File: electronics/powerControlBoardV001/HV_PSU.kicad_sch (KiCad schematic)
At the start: 0 parts

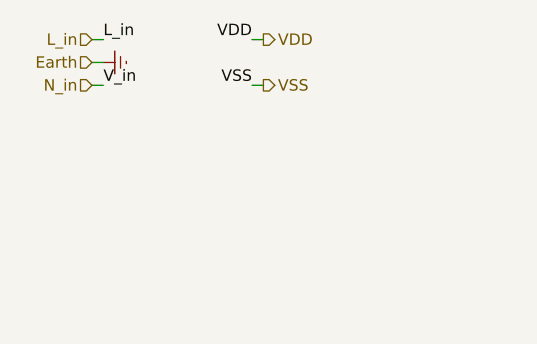
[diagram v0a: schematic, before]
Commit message: added hv psu section
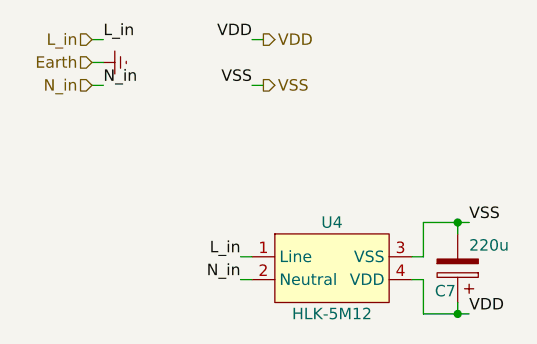
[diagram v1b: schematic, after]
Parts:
- added C7: 220u, Capacitor_THT:CP_Radial_D10.0mm_P5.00mm, symbol Device:C_Polarized
- added U4: HLK-5M12, SquantorHi-link:5MXX_series, symbol SquantorHi-link:power_module
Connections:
- net L_in: now also U4.1 (Line)
- net N_in: now also U4.2 (Neutral)
- net VDD: now also C7.1, U4.4 (VDD)
- net VSS: now also C7.2, U4.3 (VSS)
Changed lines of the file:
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@@
 (kicad_sch (version 20211123) (generator eeschema)
   (paper "A4")
+  (junction (at 60.96 48.26) (diameter 0) (color 0 0 0 0)
+  )
+  (junction (at 60.96 38.1) (diameter 0) (color 0 0 0 0)
+  )
+  (wire (pts (xy 60.96 38.1) (xy 60.96 39.37))
+    (stroke (width 0) (type default) (color 0 0 0 0))
+  )
   (wire (pts (xy 38.1 22.86) (xy 39.37 22.86))
+    (stroke (width 0) (type default) (color 0 0 0 0))
+  )
+  (wire (pts (xy 57.15 38.1) (xy 60.96 38.1))
+    (stroke (width 0) (type default) (color 0 0 0 0))
+  )
+  (wire (pts (xy 36.83 41.91) (xy 38.1 41.91))
+    (stroke (width 0) (type default) (color 0 0 0 0))
+  )
+  (wire (pts (xy 57.15 44.45) (xy 57.15 48.26))
     (stroke (width 0) (type default) (color 0 0 0 0))
   )
@@
     (stroke (width 0) (type default) (color 0 0 0 0))
   )
+  (wire (pts (xy 36.83 44.45) (xy 38.1 44.45))
+    (stroke (width 0) (type default) (color 0 0 0 0))
+  )
   (wire (pts (xy 21.59 22.86) (xy 20.32 22.86))
+    (stroke (width 0) (type default) (color 0 0 0 0))
+  )
+  (wire (pts (xy 60.96 46.99) (xy 60.96 48.26))
     (stroke (width 0) (type default) (color 0 0 0 0))
   )
@@
     (stroke (width 0) (type default) (color 0 0 0 0))
   )
+  (wire (pts (xy 60.96 48.26) (xy 62.23 48.26))
+    (stroke (width 0) (type default) (color 0 0 0 0))
+  )
+  (wire (pts (xy 57.15 41.91) (xy 57.15 38.1))
+    (stroke (width 0) (type default) (color 0 0 0 0))
+  )
+  (wire (pts (xy 55.88 41.91) (xy 57.15 41.91))
+    (stroke (width 0) (type default) (color 0 0 0 0))
+  )
+  (wire (pts (xy 55.88 44.45) (xy 57.15 44.45))
+    (stroke (width 0) (type default) (color 0 0 0 0))
+  )
+  (wire (pts (xy 57.15 48.26) (xy 60.96 48.26))
+    (stroke (width 0) (type default) (color 0 0 0 0))
+  )
+  (wire (pts (xy 60.96 38.1) (xy 62.23 38.1))
+    (stroke (width 0) (type default) (color 0 0 0 0))
+  )
   (label "VSS" (at 38.1 22.86 180)
     (effects (font (size 1.27 1.27)) (justify right bottom))
   )
-  (label "V_in" (at 21.59 22.86 0)
+  (label "L_in" (at 36.83 41.91 180)
+    (effects (font (size 1.27 1.27)) (justify right bottom))
+  )
+  (label "VSS" (at 62.23 38.1 0)
+    (effects (font (size 1.27 1.27)) (justify left bottom))
+  )
+  (label "N_in" (at 21.59 22.86 0)
     (effects (font (size 1.27 1.27)) (justify left bottom))
   )
@@
   (label "VDD" (at 38.1 17.78 180)
     (effects (font (size 1.27 1.27)) (justify right bottom))
+  )
+  (label "N_in" (at 36.83 44.45 180)
+    (effects (font (size 1.27 1.27)) (justify right bottom))
+  )
+  (label "VDD" (at 62.23 48.26 0)
+    (effects (font (size 1.27 1.27)) (justify left bottom))
   )
   (hierarchical_label "VSS" (shape output) (at 39.37 22.86 0)
@@
     (pin "1")
   )
+  (symbol (lib_id "SquantorHi-link:power_module") (at 46.99 43.18 0) (unit 1)
+    (in_bom yes) (on_board yes)
+    (property "Reference" "U4" (id 0) (at 46.99 38.1 0))
+    (property "Value" "HLK-5M12" (id 1) (at 46.99 48.26 0))
+    (property "Footprint" "SquantorHi-link:5MXX_series" (id 2) (at 46.99 43.18 0)
+      (effects (font (size 1.27 1.27)) hide)
+    )
+    (property "Datasheet" "" (id 3) (at 46.99 43.18 0)
+      (effects (font (size 1.27 1.27)) hide)
+    )
+    (pin "1")
+    (pin "2")
+    (pin "3")
+    (pin "4")
+  )
+  (symbol (lib_id "Device:C_Polarized") (at 60.96 43.18 180) (unit 1)
+    (in_bom yes) (on_board yes)
+    (property "Reference" "C7" (id 0) (at 58.42 45.72 0)
+      (effects (font (size 1.27 1.27)) (justify right))
+    )
+    (property "Value" "220u" (id 1) (at 62.23 40.64 0)
+      (effects (font (size 1.27 1.27)) (justify right))
+    )
+    (property "Footprint" "Capacitor_THT:CP_Radial_D10.0mm_P5.00mm" (id 2) (at 59.9948 39.37 0)
+      (effects (font (size 1.27 1.27)) hide)
+    )
+    (property "Datasheet" "~" (id 3) (at 60.96 43.18 0)
+      (effects (font (size 1.27 1.27)) hide)
+    )
+    (pin "1")
+    (pin "2")
+  )
 )
